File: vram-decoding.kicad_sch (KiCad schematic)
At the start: 7 parts, among them U2 74HCT04, U3 74HCT574, U4 74HCT574, U5 74HCT574

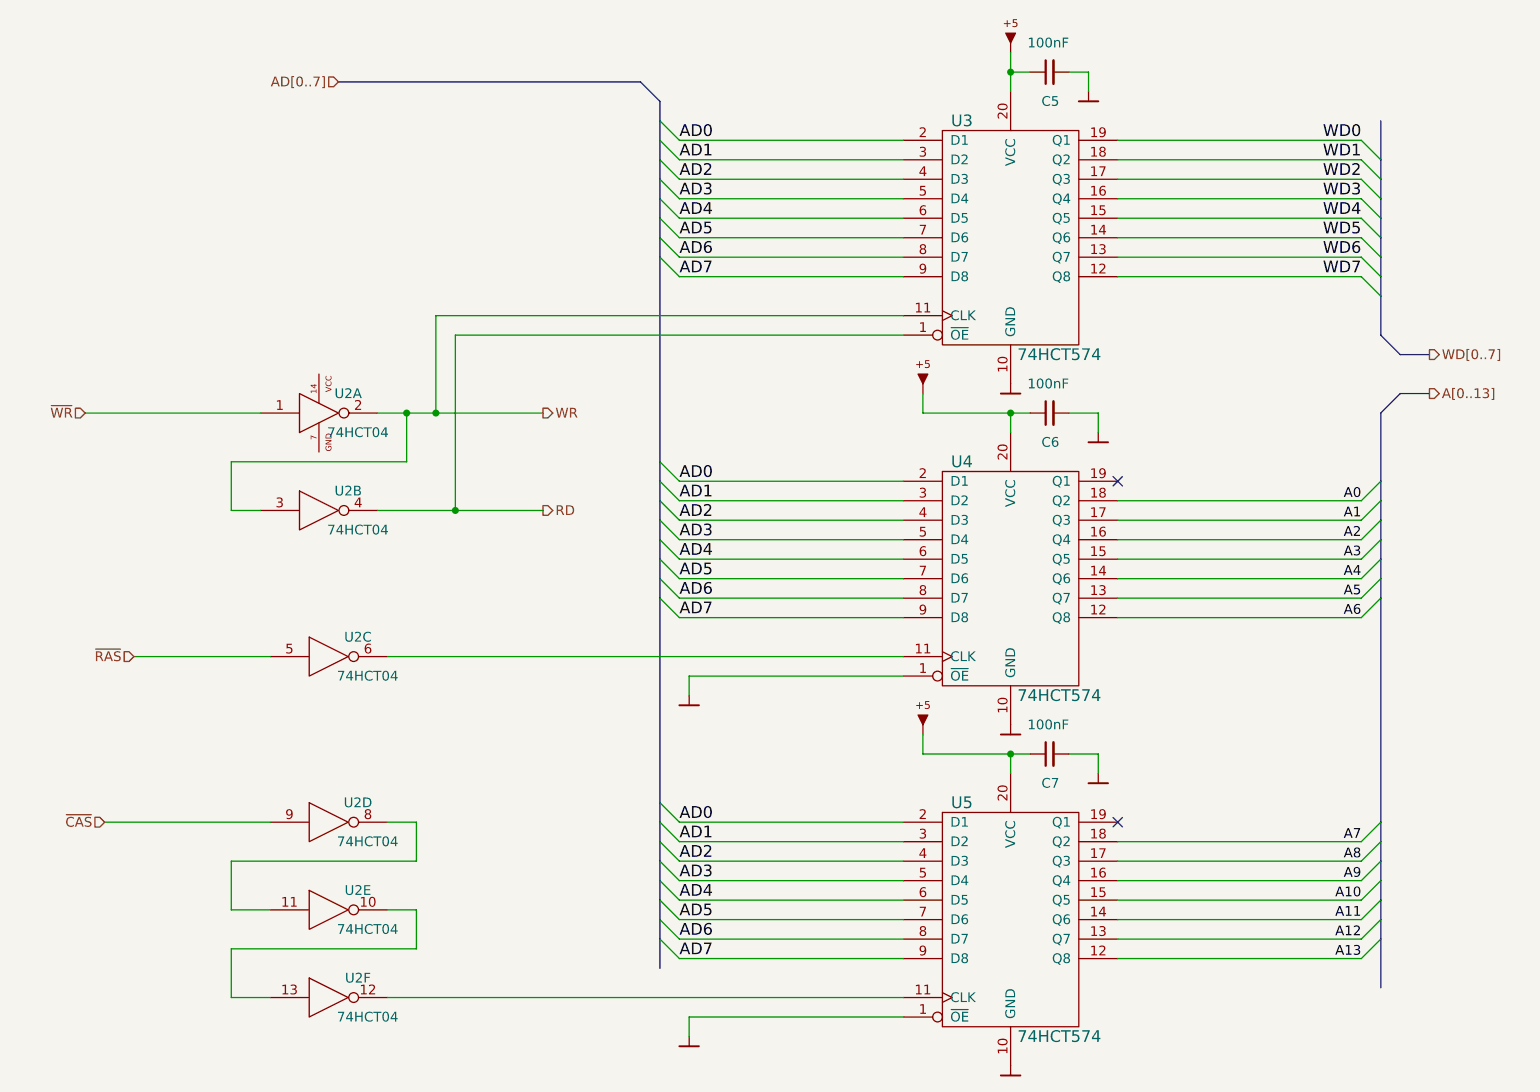
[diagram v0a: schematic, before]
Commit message: Update to latest Artemisa kicadlibs
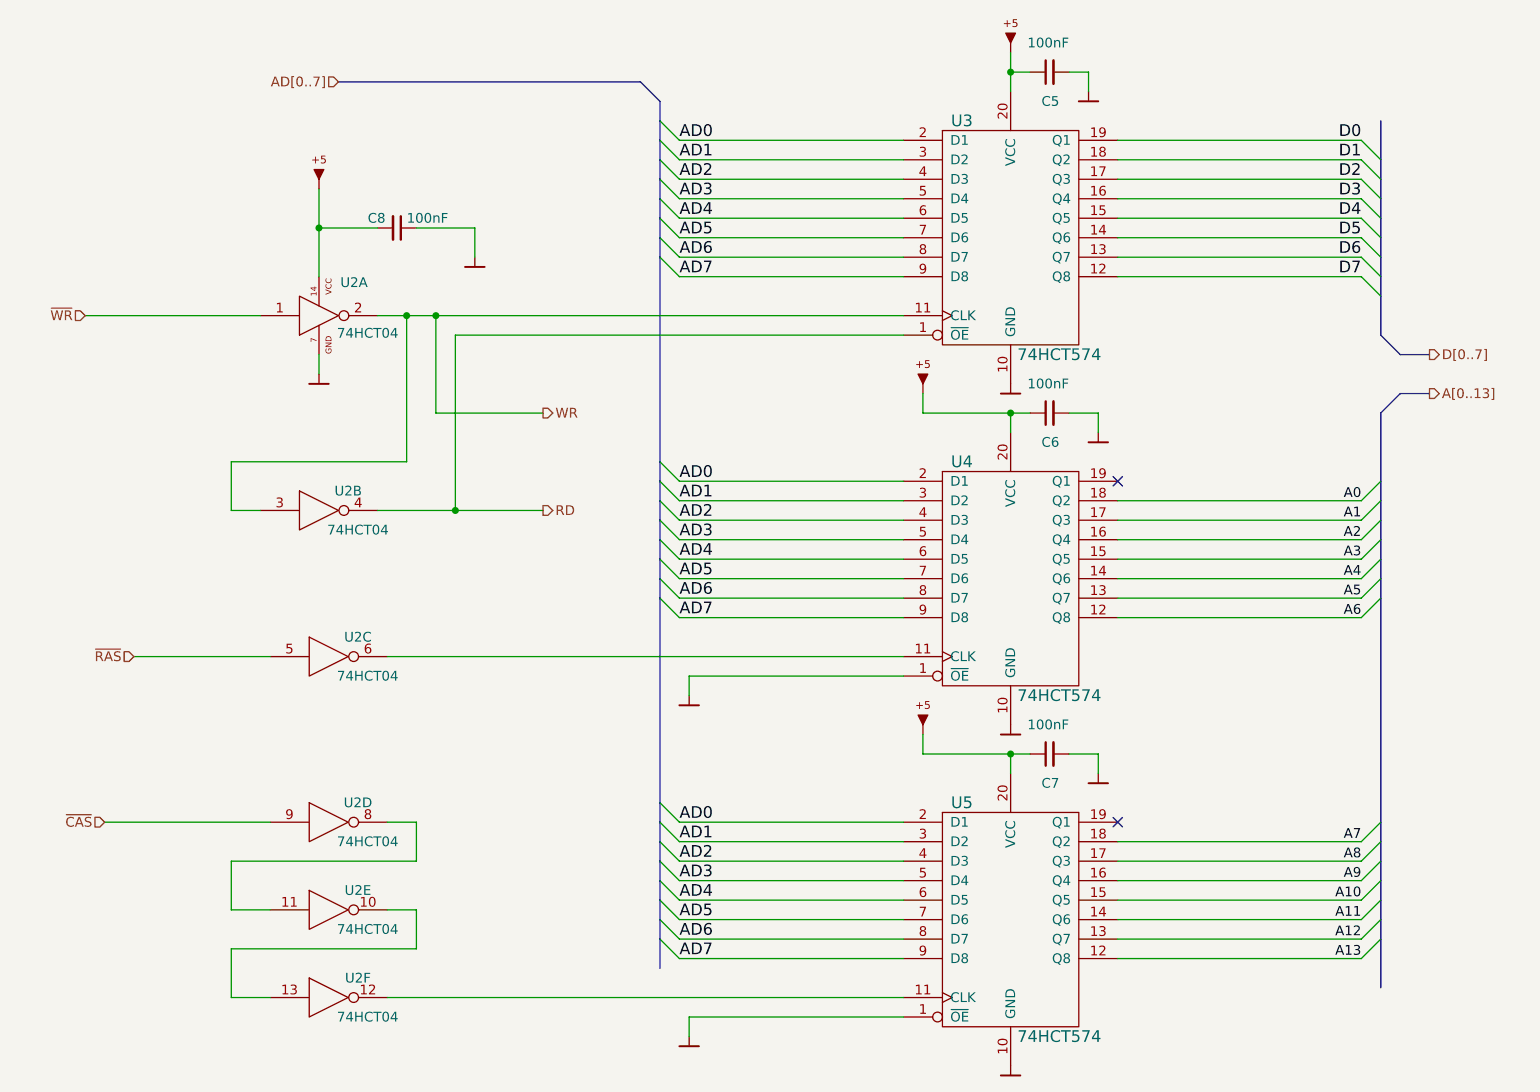
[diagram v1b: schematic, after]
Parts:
- added C8: 100nF, artemisa:Disc_capacitor, symbol artemisa:Cap
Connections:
- net GND: now also U2.7 (GND), C8.1
- net VCC: now also U2.14 (VCC), C8.2
- net WD0 renamed D0
- net WD1 renamed D1
- net WD2 renamed D2
- net WD3 renamed D3
- net WD4 renamed D4
- net WD5 renamed D5
- net WD6 renamed D6
- net WD7 renamed D7
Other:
- moved on the sheet: U2A

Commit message: Use spare MCP6294 as CSYNC buffer
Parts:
- C5, C6, C7, C8: footprint artemisa:Disc_capacitor -> PCM_artemisa:Disc_capacitor
- U2: footprint artemisa:DIP-14_300 -> PCM_artemisa:DIP-14_300
- U3, U4, U5: footprint artemisa:DIP-20_300 -> PCM_artemisa:DIP-20_300
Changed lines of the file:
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@@
 			)
 		)
-		(property "Footprint" "artemisa:DIP-14_300"
+		(property "Footprint" "PCM_artemisa:DIP-14_300"
 			(at 58.42 60.96 0)
 			(hide yes)
@@
 			)
 		)
-		(property "Footprint" "artemisa:DIP-14_300"
+		(property "Footprint" "PCM_artemisa:DIP-14_300"
 			(at 58.42 86.36 0)
 			(hide yes)
@@
 			)
 		)
-		(property "Footprint" "artemisa:DIP-14_300"
+		(property "Footprint" "PCM_artemisa:DIP-14_300"
 			(at 59.69 105.41 0)
 			(hide yes)
@@
 			)
 		)
-		(property "Footprint" "artemisa:DIP-14_300"
+		(property "Footprint" "PCM_artemisa:DIP-14_300"
 			(at 59.69 127 0)
 			(hide yes)
@@
 			)
 		)
-		(property "Footprint" "artemisa:DIP-14_300"
+		(property "Footprint" "PCM_artemisa:DIP-14_300"
 			(at 59.69 138.43 0)
 			(hide yes)
@@
 			)
 		)
-		(property "Footprint" "artemisa:DIP-14_300"
+		(property "Footprint" "PCM_artemisa:DIP-14_300"
 			(at 59.69 149.86 0)
 			(hide yes)
@@
 			)
 		)
-		(property "Footprint" "artemisa:DIP-20_300"
+		(property "Footprint" "PCM_artemisa:DIP-20_300"
 			(at 148.59 57.15 0)
 			(hide yes)
@@
 			)
 		)
-		(property "Footprint" "artemisa:DIP-20_300"
+		(property "Footprint" "PCM_artemisa:DIP-20_300"
 			(at 148.59 101.6 0)
 			(hide yes)
@@
 			)
 		)
-		(property "Footprint" "artemisa:DIP-20_300"
+		(property "Footprint" "PCM_artemisa:DIP-20_300"
 			(at 148.59 146.05 0)
 			(hide yes)
@@
 			)
 		)
-		(property "Footprint" "artemisa:Disc_capacitor"
+		(property "Footprint" "PCM_artemisa:Disc_capacitor"
 			(at 153.67 73.66 0)
 			(hide yes)
@@
 			)
 		)
-		(property "Footprint" "artemisa:Disc_capacitor"
+		(property "Footprint" "PCM_artemisa:Disc_capacitor"
 			(at 153.67 118.11 0)
 			(hide yes)
@@
 			)
 		)
-		(property "Footprint" "artemisa:Disc_capacitor"
+		(property "Footprint" "PCM_artemisa:Disc_capacitor"
 			(at 153.67 29.21 0)
 			(hide yes)
@@
 			)
 		)
-		(property "Footprint" "artemisa:Disc_capacitor"
+		(property "Footprint" "PCM_artemisa:Disc_capacitor"
 			(at 68.58 49.53 0)
 			(hide yes)
